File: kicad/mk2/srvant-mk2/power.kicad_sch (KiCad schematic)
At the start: 69 parts, among them J1 Barrel_Jack_Switch, J2 Conn_01x02, Q1 DMP3013SFV-7, U1 AP63205WU, U13 RT9742SNGV, U15 TLV62585DRLR, U2 AP64501SP-13, U3 74AHC1G32, U4 INA219AxDCN

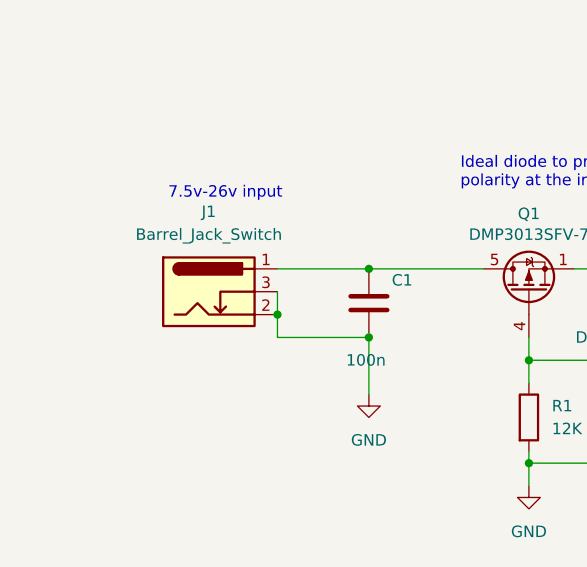
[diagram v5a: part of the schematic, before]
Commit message: replace power jack, change board dimentions, small fixes
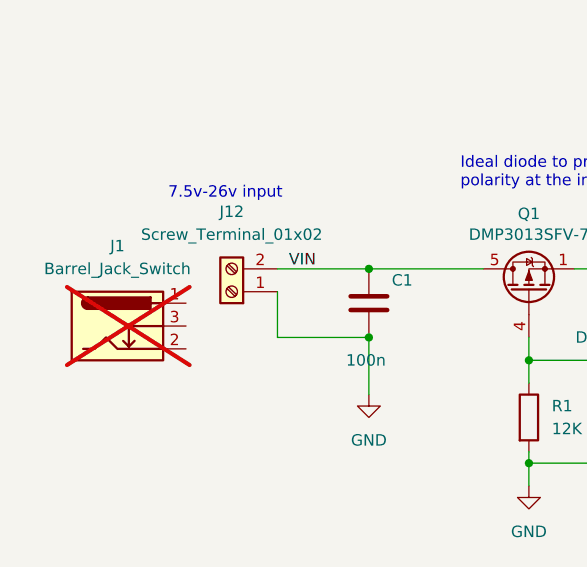
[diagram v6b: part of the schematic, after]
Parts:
- added J12: Screw_Terminal_01x02, TerminalBlock:TerminalBlock_bornier-2_P5.08mm, symbol ARJM11:Screw_Terminal_01x02
- J1: now not fitted; now left out of the parts list
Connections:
- net GND: now also J12.1 (Pin_1); no longer J1.2, J1.3
- net VIN: now reaches C1.1, Q1.5 (D)
- net VIN: now also J12.2 (Pin_2); no longer J1.1
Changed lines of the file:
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@@
   (junction (at 124.46 167.64) (diameter 0) (color 0 0 0 0)
-  )
-  (junction (at 48.26 116.84) (diameter 0) (color 0 0 0 0)
   )
   (junction (at 190.754 243.84) (diameter 0.9144) (color 0 0 0 0)
@@
     (stroke (width 0) (type default))
   )
-  (wire (pts (xy 48.26 114.3) (xy 48.26 116.84))
+  (wire (pts (xy 48.26 114.3) (xy 48.26 119.38))
     (stroke (width 0) (type default))
   )
@@
   )
   (wire (pts (xy 143.51 119.38) (xy 137.16 119.38))
-    (stroke (width 0) (type default))
-  )
-  (wire (pts (xy 48.26 116.84) (xy 48.26 119.38))
     (stroke (width 0) (type default))
   )
@@
   (label "BMC_HOST_POWER_EN" (at 323.85 144.78 180) (fields_autoplaced)
     (effects (font (size 1.27 1.27)) (justify right bottom))
+  )
+  (label "VIN" (at 49.53 111.76 0) (fields_autoplaced)
+    (effects (font (size 1.27 1.27)) (justify left bottom))
   )
   (label "+5v_HOST" (at 100.33 255.27 180) (fields_autoplaced)
@@
     )
   )
+  (symbol (lib_id "ARJM11:Screw_Terminal_01x02") (at 43.18 114.3 180) (unit 1)
+    (in_bom yes) (on_board yes) (dnp no) (fields_autoplaced)
+    (property "Reference" "J12" (at 43.18 105.41 0)
+      (effects (font (size 1.27 1.27)))
+    )
+    (property "Value" "Screw_Terminal_01x02" (at 43.18 107.95 0)
+      (effects (font (size 1.27 1.27)))
+    )
+    (property "Footprint" "TerminalBlock:TerminalBlock_bornier-2_P5.08mm" (at 43.18 114.3 0)
+      (effects (font (size 1.27 1.27)) hide)
+    )
+    (property "Datasheet" "~" (at 43.18 114.3 0)
+      (effects (font (size 1.27 1.27)) hide)
+    )
+    (property "manf#" "" (at 43.18 114.3 0)
+      (effects (font (size 1.27 1.27)) hide)
+    )
+    (property "digikey#" "" (at 43.18 114.3 0)
+      (effects (font (size 1.27 1.27)) hide)
+    )
+    (property "mouser#" "" (at 43.18 114.3 0)
+      (effects (font (size 1.27 1.27)) hide)
+    )
+    (property "farnell#" "" (at 43.18 114.3 0)
+      (effects (font (size 1.27 1.27)) hide)
+    )
+    (property "rs#" "" (at 43.18 114.3 0)
+      (effects (font (size 1.27 1.27)) hide)
+    )
+    (property "Part Description" "" (at 43.18 114.3 0)
+      (effects (font (size 1.27 1.27)) hide)
+    )
+    (pin "1")
+    (pin "2")
+    (instances
+      (project "srvant-mk2"
+        (path "/1859a578-b791-4142-bdf4-fda494df1146/c300a602-5caa-44c4-bd60-e0bac469451e"
+          (reference "J12") (unit 1)
+        )
+      )
+    )
+  )
   (symbol (lib_id "Device:C") (at 91.44 118.11 0) (unit 1)
     (in_bom yes) (on_board yes) (dnp no) (fields_autoplaced)
@@
     )
   )
+  (symbol (lib_id "ARJM11:Barrel_Jack_Switch") (at 30.48 118.11 0) (unit 1)
+    (in_bom no) (on_board no) (dnp yes) (fields_autoplaced)
+    (property "Reference" "J1" (at 30.48 109.22 0)
+      (effects (font (size 1.27 1.27)))
+    )
+    (property "Value" "Barrel_Jack_Switch" (at 30.48 111.76 0)
+      (effects (font (size 1.27 1.27)))
+    )
+    (property "Footprint" "Connector_BarrelJack:BarrelJack_Horizontal" (at 31.75 119.126 0)
+      (effects (font (size 1.27 1.27)) hide)
+    )
+    (property "Datasheet" "https://www.we-online.com/catalog/datasheet/694106301002.pdf" (at 31.75 119.126 0)
+      (effects (font (size 1.27 1.27)) hide)
+    )
+    (property "manf#" "694106301002 " (at 30.48 118.11 0)
+      (effects (font (size 1.27 1.27)) hide)
+    )
+    (property "digikey#" "" (at 30.48 118.11 0)
+      (effects (font (size 1.27 1.27)) hide)
+    )
+    (property "mouser#" " 710-694106301002 " (at 30.48 118.11 0)
+      (effects (font (size 1.27 1.27)) hide)
+    )
+    (property "farnell#" "" (at 30.48 118.11 0)
+      (effects (font (size 1.27 1.27)) hide)
+    )
+    (property "rs#" "" (at 30.48 118.11 0)
+      (effects (font (size 1.27 1.27)) hide)
+    )
+    (property "Part Description" "" (at 30.48 118.11 0)
+      (effects (font (size 1.27 1.27)) hide)
+    )
+    (property "Sim.Enable" "0" (at 30.48 118.11 0)
+      (effects (font (size 1.27 1.27)) hide)
+    )
+    (pin "1")
+    (pin "2")
+    (pin "3")
+    (instances
+      (project "srvant-mk2"
+        (path "/1859a578-b791-4142-bdf4-fda494df1146/c300a602-5caa-44c4-bd60-e0bac469451e"
+          (reference "J1") (unit 1)
+        )
+      )
+    )
+  )
   (symbol (lib_id "Device:C") (at 232.41 101.6 0) (unit 1)
     (in_bom yes) (on_board yes) (dnp no)
@@
         )
       )
-    )
-  )
-  (symbol (lib_id "ARJM11:Barrel_Jack_Switch") (at 40.64 114.3 0) (unit 1)
-    (in_bom yes) (on_board yes) (dnp no) (fields_autoplaced)
-    (property "Reference" "J1" (at 40.64 105.41 0)
-      (effects (font (size 1.27 1.27)))
-    )
-    (property "Value" "Barrel_Jack_Switch" (at 40.64 107.95 0)
-      (effects (font (size 1.27 1.27)))
-    )
-    (property "Footprint" "Connector_BarrelJack:BarrelJack_Horizontal" (at 41.91 115.316 0)
-      (effects (font (size 1.27 1.27)) hide)
-    )
-    (property "Datasheet" "https://www.we-online.com/catalog/datasheet/694106301002.pdf" (at 41.91 115.316 0)
-      (effects (font (size 1.27 1.27)) hide)
-    )
-    (property "manf#" "694106301002 " (at 40.64 114.3 0)
-      (effects (font (size 1.27 1.27)) hide)
-    )
-    (property "digikey#" "" (at 40.64 114.3 0)
-      (effects (font (size 1.27 1.27)) hide)
-    )
-    (property "mouser#" " 710-694106301002 " (at 40.64 114.3 0)
-      (effects (font (size 1.27 1.27)) hide)
-    )
-    (property "farnell#" "" (at 40.64 114.3 0)
-      (effects (font (size 1.27 1.27)) hide)
-    )
-    (property "rs#" "" (at 40.64 114.3 0)
-      (effects (font (size 1.27 1.27)) hide)
-    )
-    (property "Part Description" "" (at 40.64 114.3 0)
-      (effects (font (size 1.27 1.27)) hide)
-    )
-    (pin "1")
-    (pin "2")
-    (pin "3")
-    (instances
-      (project "srvant-mk2"
-        (path "/1859a578-b791-4142-bdf4-fda494df1146/c300a602-5caa-44c4-bd60-e0bac469451e"
-          (reference "J1") (unit 1)
-        )
-      )

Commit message: add more 3d models, add layer indication, update readme
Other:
- moved on the sheet: J12
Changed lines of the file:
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@@
     (stroke (width 0) (type default))
   )
-  (wire (pts (xy 48.26 111.76) (xy 58.42 111.76))
+  (wire (pts (xy 46.99 111.76) (xy 58.42 111.76))
     (stroke (width 0) (type default))
   )
@@
     (stroke (width 0) (type default))
   )
-  (wire (pts (xy 48.26 114.3) (xy 48.26 119.38))
+  (wire (pts (xy 46.99 114.3) (xy 46.99 119.38))
     (stroke (width 0) (type default))
   )
@@
     (stroke (width 0) (type default))
   )
-  (wire (pts (xy 48.26 119.38) (xy 58.42 119.38))
+  (wire (pts (xy 46.99 119.38) (xy 58.42 119.38))
     (stroke (width 0) (type default))
   )
@@
     )
   )
-  (symbol (lib_id "ARJM11:Screw_Terminal_01x02") (at 43.18 114.3 180) (unit 1)
+  (symbol (lib_id "ARJM11:Screw_Terminal_01x02") (at 41.91 114.3 180) (unit 1)
     (in_bom yes) (on_board yes) (dnp no) (fields_autoplaced)
-    (property "Reference" "J12" (at 43.18 105.41 0)
+    (property "Reference" "J12" (at 41.91 105.41 0)
       (effects (font (size 1.27 1.27)))
     )
-    (property "Value" "Screw_Terminal_01x02" (at 43.18 107.95 0)
+    (property "Value" "Screw_Terminal_01x02" (at 41.91 107.95 0)
       (effects (font (size 1.27 1.27)))
     )
-    (property "Footprint" "TerminalBlock:TerminalBlock_bornier-2_P5.08mm" (at 43.18 114.3 0)
-      (effects (font (size 1.27 1.27)) hide)
-    )
-    (property "Datasheet" "~" (at 43.18 114.3 0)
-      (effects (font (size 1.27 1.27)) hide)
-    )
-    (property "manf#" "" (at 43.18 114.3 0)
-      (effects (font (size 1.27 1.27)) hide)
-    )
-    (property "digikey#" "" (at 43.18 114.3 0)
-      (effects (font (size 1.27 1.27)) hide)
-    )
-    (property "mouser#" "" (at 43.18 114.3 0)
-      (effects (font (size 1.27 1.27)) hide)
-    )
-    (property "farnell#" "" (at 43.18 114.3 0)
-      (effects (font (size 1.27 1.27)) hide)
-    )
-    (property "rs#" "" (at 43.18 114.3 0)
-      (effects (font (size 1.27 1.27)) hide)
-    )
-    (property "Part Description" "" (at 43.18 114.3 0)
-      (effects (font (size 1.27 1.27)) hide)
-    )
+    (property "Footprint" "TerminalBlock:TerminalBlock_bornier-2_P5.08mm" (at 41.91 114.3 0)
+      (effects (font (size 1.27 1.27)) hide)
+    )
+    (property "Datasheet" "~" (at 41.91 114.3 0)
+      (effects (font (size 1.27 1.27)) hide)
+    )
+    (property "manf#" "" (at 41.91 114.3 0)
+      (effects (font (size 1.27 1.27)) hide)
+    )
+    (property "digikey#" "" (at 41.91 114.3 0)
+      (effects (font (size 1.27 1.27)) hide)
+    )
+    (property "mouser#" "" (at 41.91 114.3 0)
+      (effects (font (size 1.27 1.27)) hide)
+    )
+    (property "farnell#" "" (at 41.91 114.3 0)
+      (effects (font (size 1.27 1.27)) hide)
+    )
+    (property "rs#" "" (at 41.91 114.3 0)
+      (effects (font (size 1.27 1.27)) hide)
+    )
+    (property "Part Description" "" (at 41.91 114.3 0)
+      (effects (font (size 1.27 1.27)) hide)
+    )

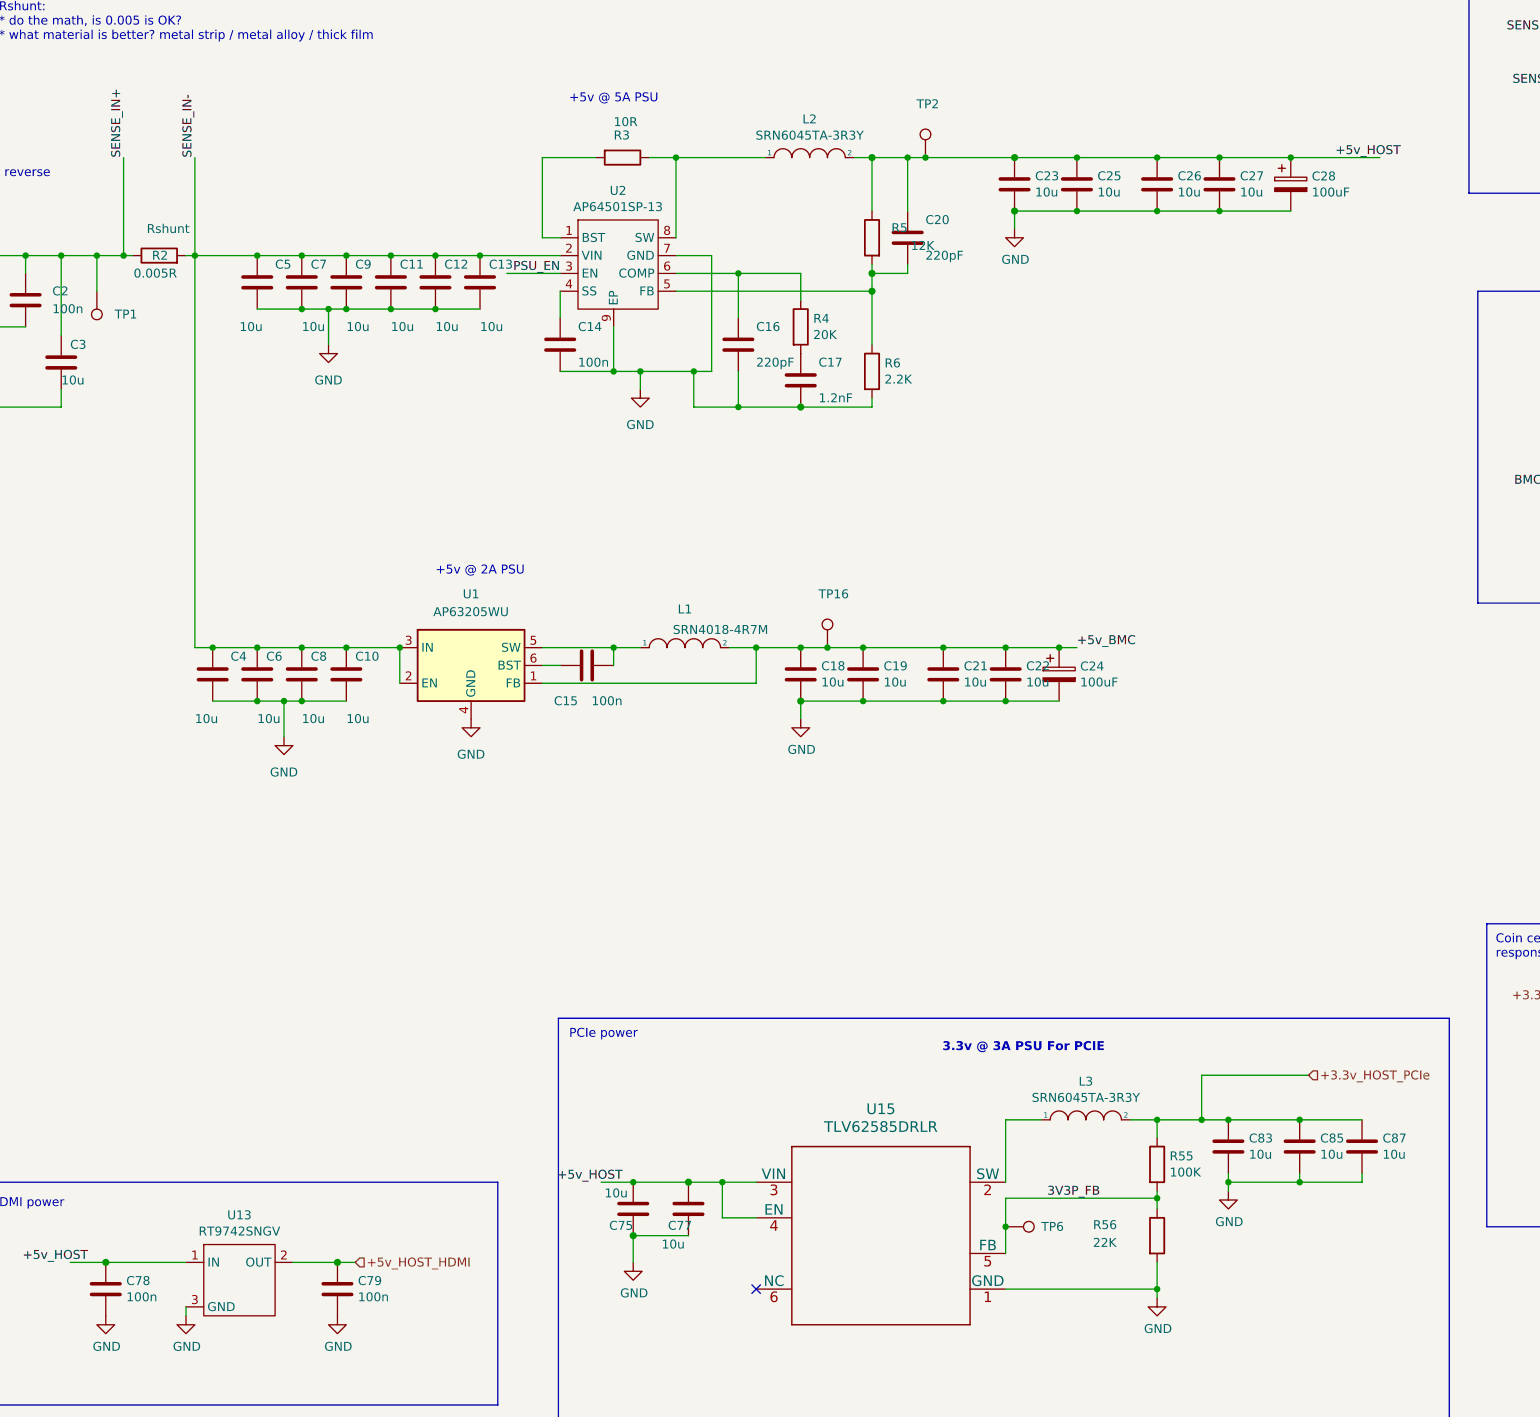
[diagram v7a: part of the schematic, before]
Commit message: add rp-t113-s3 datasheets (cn), make CI happier
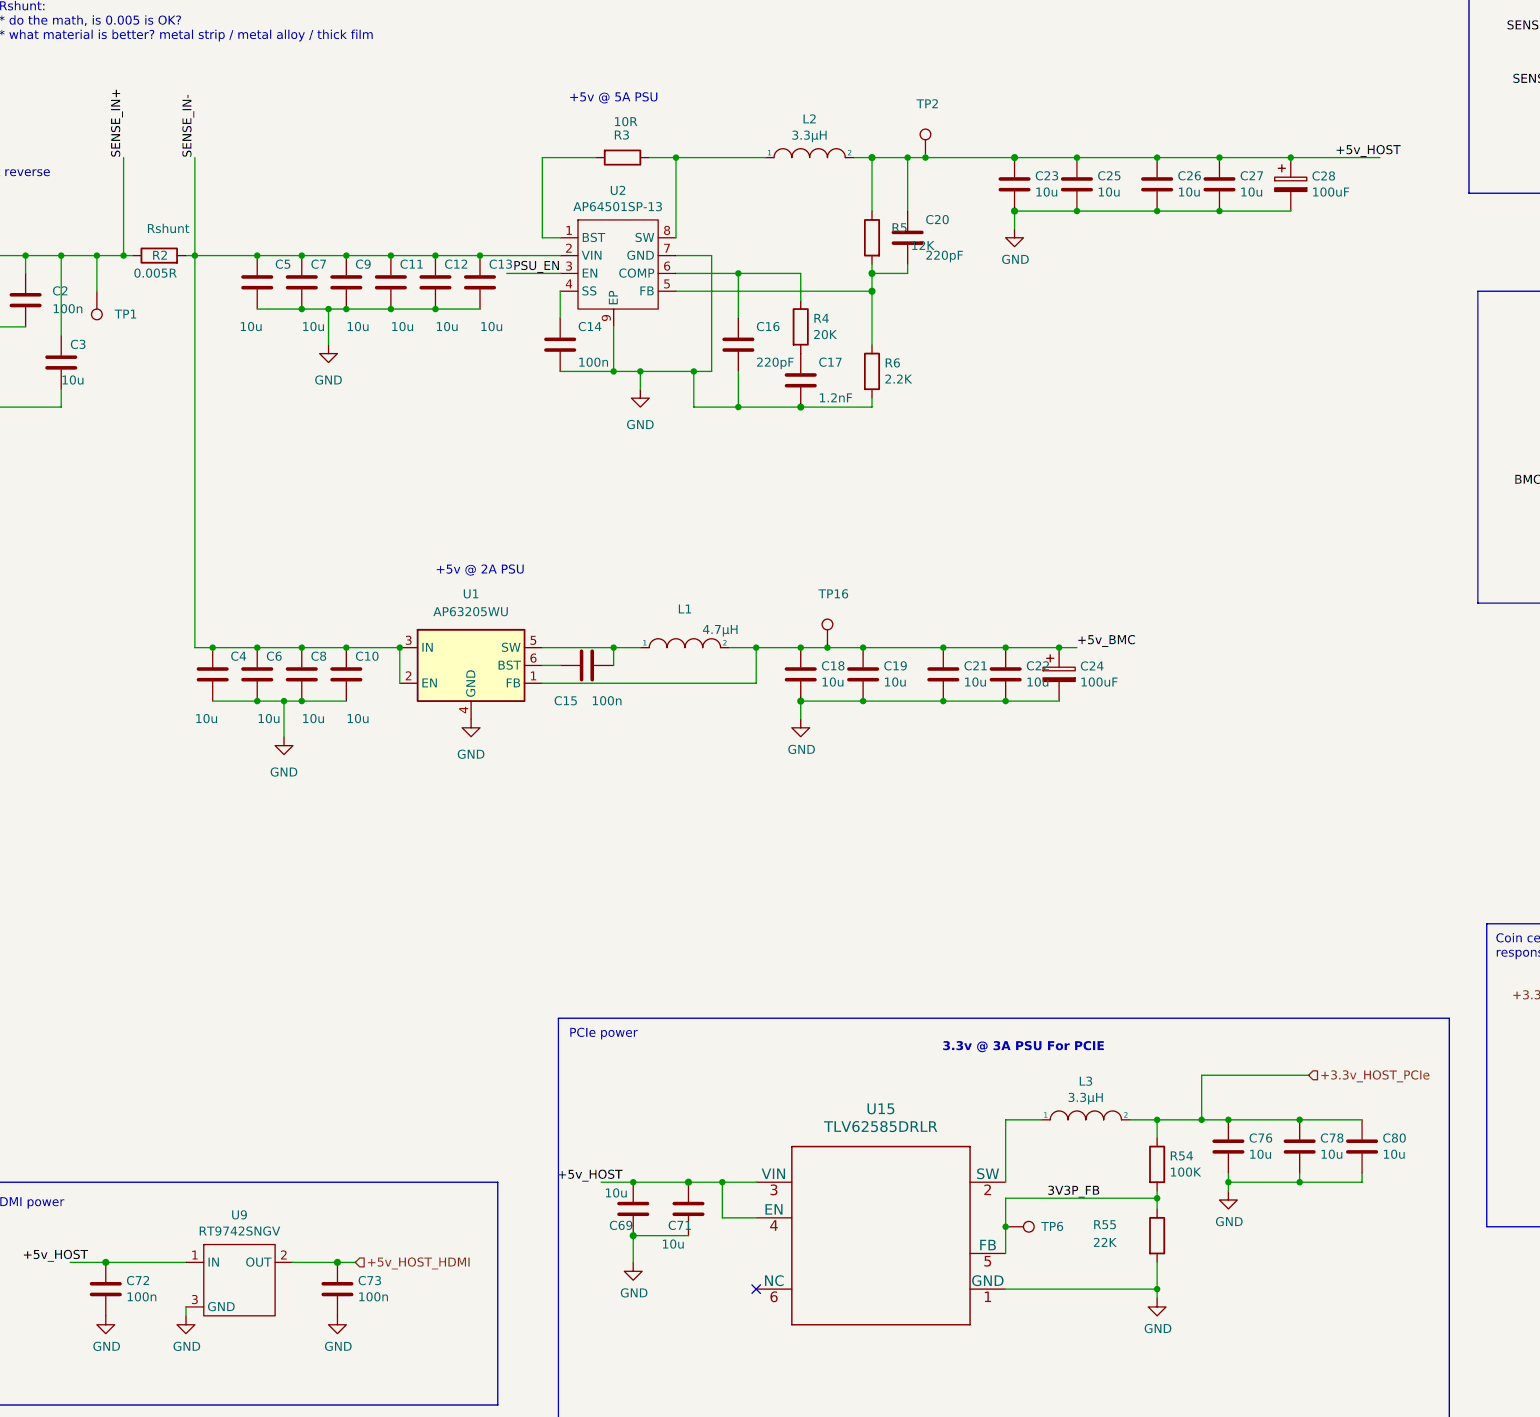
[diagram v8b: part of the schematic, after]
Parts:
- C10, C11, C12, C13, C3, C30, C4, C5, C6, C7, C8, C9: manf# GRM21BC8YA106KE11L -> GRM21BC8YA106KE11L
- C14, C15, C29: mouser# 963-EMK105B7104KV-F -> 963-EMK105B7104KV-F
- C69: renamed from C75; Field6 GRM21BC8YA106KE11L -> GRM21BC8YA106KE11L; Part Description 10uF 10% or 20% 35V Ceramic Capacitor X6S 0805 (2012 Metric) -> 10uF 10% 10V Ceramic Capacitor X7R 0805 (2012 Metric); digikey# (none) -> 490-14381-1-ND; manf# (none) -> GRM21BR71A106KA73L
- C71: renamed from C77; Field6 GRM21BC8YA106KE11L -> GRM21BC8YA106KE11L; Part Description 10uF 10% or 20% 35V Ceramic Capacitor X6S 0805 (2012 Metric) -> 10uF 10% 10V Ceramic Capacitor X7R 0805 (2012 Metric); digikey# (none) -> 490-14381-1-ND; manf# (none) -> GRM21BR71A106KA73L
- C76: renamed from C83; digikey# (none) -> 490-14381-1-ND; manf# (none) -> GRM21BR71A106KA73L
- C78: renamed from C85; digikey# (none) -> 490-14381-1-ND; manf# (none) -> GRM21BR71A106KA73L
- C80: renamed from C87; digikey# (none) -> 490-14381-1-ND; manf# (none) -> GRM21BR71A106KA73L
- J1: manf# 694106301002 -> 694106301002; mouser# 710-694106301002 -> 710-694106301002
- L1: value SRN4018-4R7M -> 4.7µH
- L2, L3: value SRN6045TA-3R3Y -> 3.3µH
- Q1: mouser# 621-DMP3013SFV-7 -> 621-DMP3013SFV-7
- R2: Part Description Rshunt -> Rshunt
- R55: renamed from R56; Field6 RK73G1ETQTP4702D -> RK73G1ETQTP4702D
- R6: manf# RK73G1ETQTP2201D -> RK73G1ETQTP2201D
- U1: mouser# 621-AP63205WU-7 -> 621-AP63205WU-7
- U15: manf# TLV62585DRLR -> TLV62585DRLR; mouser# 595-TLV62585DRLR -> 595-TLV62585DRLR
- U4: manf# INA219AIDCNR -> INA219AIDCNR; mouser# 595-INA219AIDCNR -> 595-INA219AIDCNR
- renumbered C78 to C72, C79 to C73, R55 to R54, U13 to U9
